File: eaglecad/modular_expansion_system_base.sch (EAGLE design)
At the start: 34 parts, among them IC1 74LS244N, IC10 74LS30N, IC2 74LS244N, IC3 74LS244N, IC4 SRAM, IC5 74LS30N, IC8 74LS00N, IC9 7805T, J1-INTERRUPTS INTERRUPTS, J1_ADDRESS_CON j1, J2-WAITS WAITS, J2_DATA_AND_POWER_CON j2, SW1 100SP3T1B1M6QE

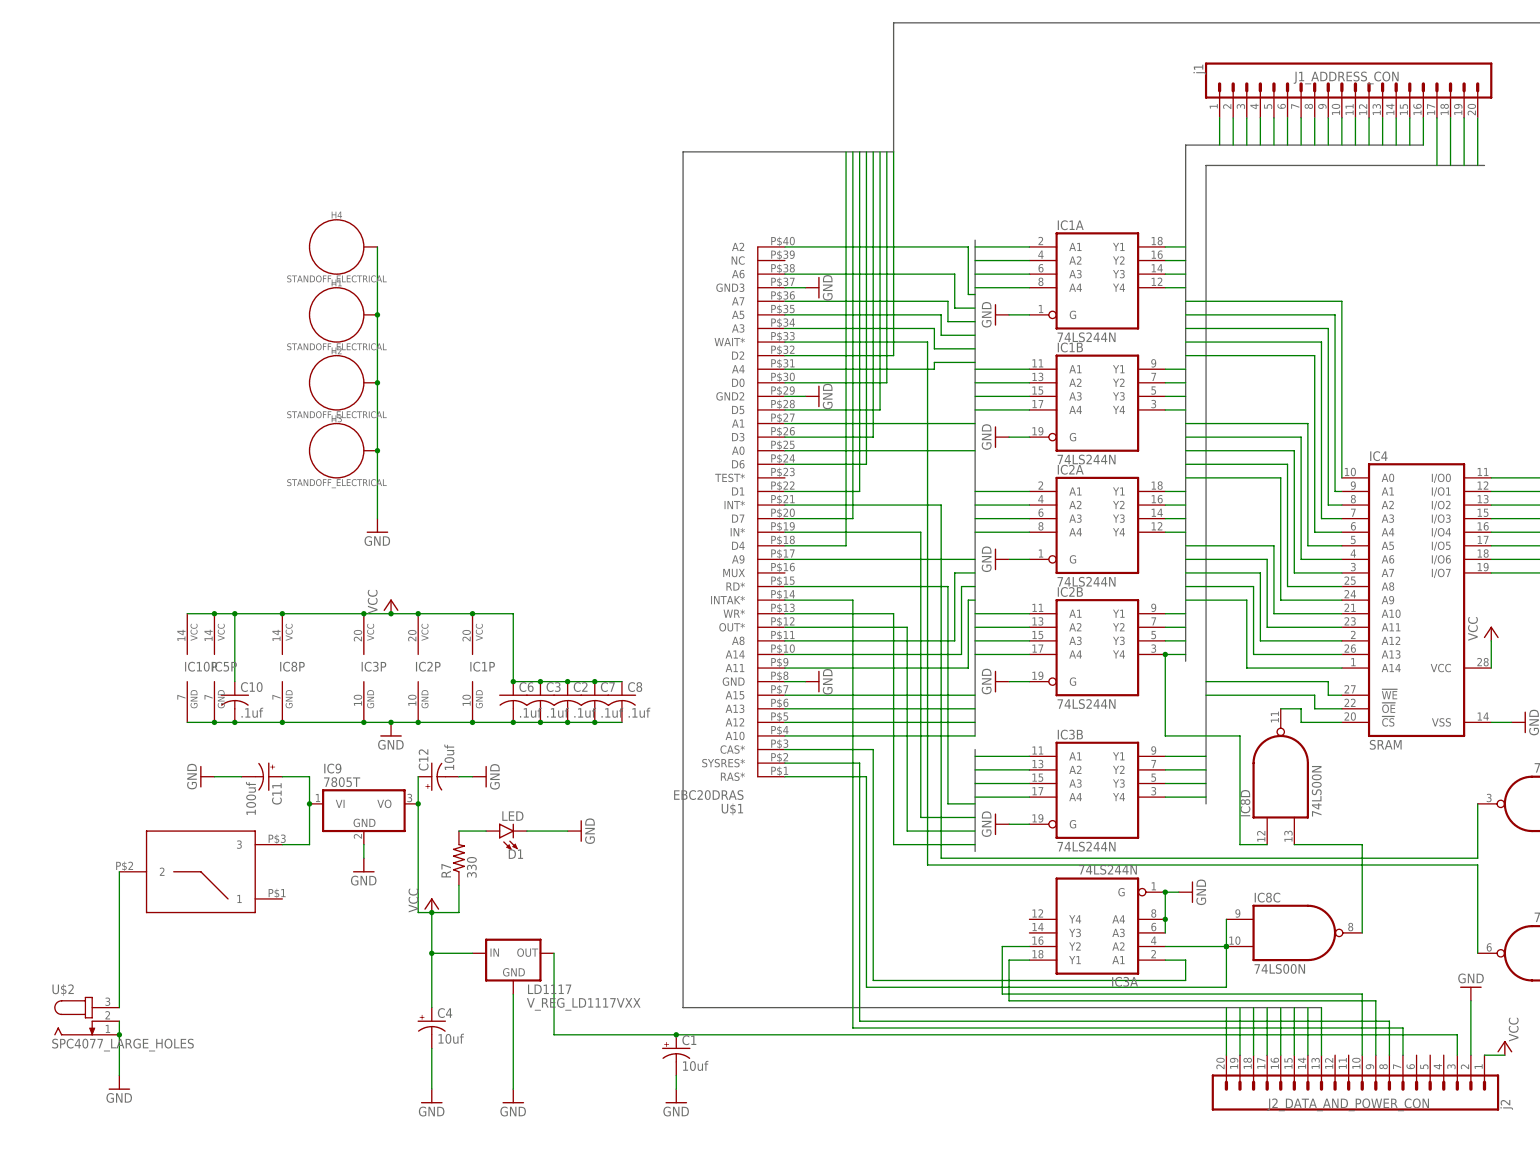
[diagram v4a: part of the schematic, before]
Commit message: added switching supply to base pcb
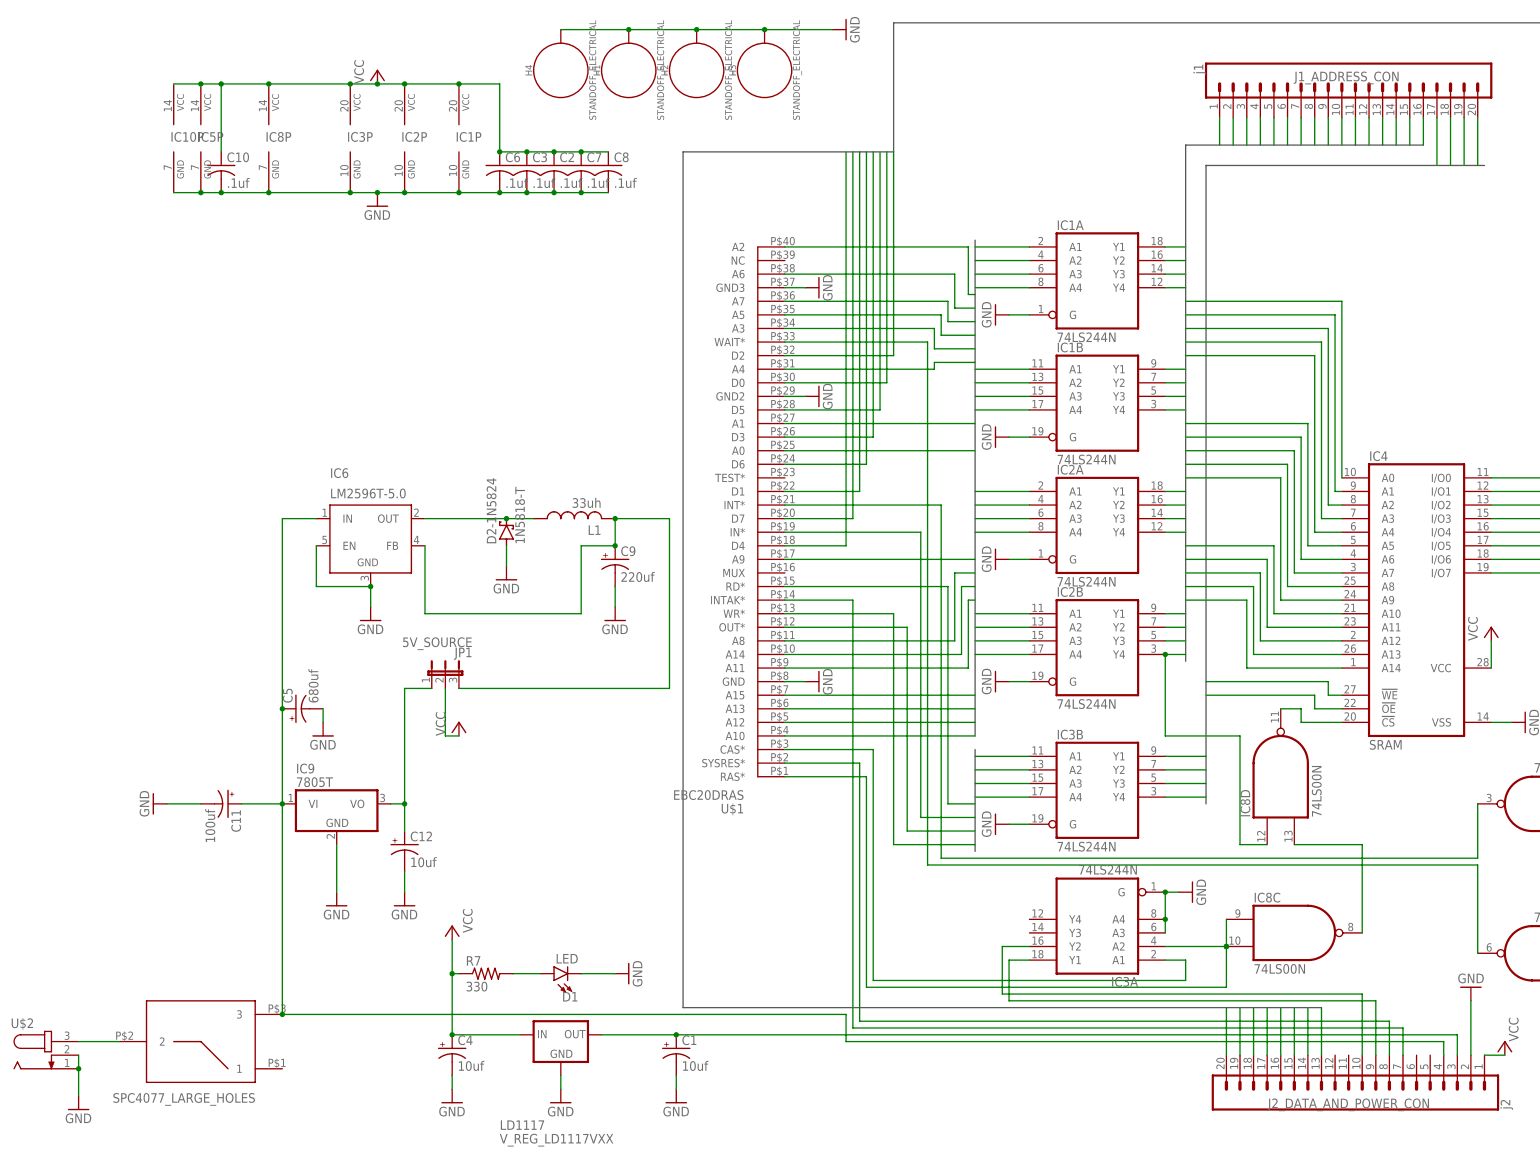
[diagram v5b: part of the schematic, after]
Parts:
- added C5: 680uf, rcl:CPOL-USE2.5-5
- added C9: 220uf, rcl:CPOL-USE2.5-5
- added D2-1N5824: 1N5818-T, diode:1N5818-T
- added IC6: LM2596T-5.0, linear:LM2596TH
- added JP1: 5V_SOURCE, jumper:JP2E
- added L1: 33uh, rcl:L-US6000-XXX-RC
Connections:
- net N$3 renamed 9V-IN
- removed net VOLTAGE-IN: C11.+, IC9.VI, SW1.3
- new net 5V_FROM_LINEAR_REG: C12.+, IC9.VO, JP1.1
- new net 5V_FROM_SWITCHER: C9.+, IC6.FB, JP1.3, L1.2
- new net 9V-POST-SW: C11.+, C5.+, IC6.IN, IC9.VI, J2_DATA_AND_POWER_CON.4, SW1.3
- new net N$1: D2-1N5824.C, IC6.OUT, L1.1
- net GND: now also C5.-, C9.-, D2-1N5824.A, IC6.EN, IC6.GND
- net VCC: now also JP1.2; no longer C12.+, IC9.VO
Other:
- moved on the sheet: C10, C11, C12, C2, C3, C4, C6, C7, C8, D1, H1, H2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

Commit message: updated schematics, boards, and pdfs
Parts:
- renumbered LD1117 to LD1117V33
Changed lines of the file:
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@@
 <setting verticaltext="up"/>
 </settings>
-<grid distance="0.05" unitdist="inch" unit="inch" style="lines" multiple="1" display="no" altdistance="0.005" altunitdist="inch" altunit="inch"/>
+<grid distance="0.1" unitdist="inch" unit="inch" style="lines" multiple="1" display="no" altdistance="0.01" altunitdist="inch" altunit="inch"/>
 <layers>
 <layer number="1" name="Top" color="4" fill="1" visible="no" active="no"/>
@@
 <part name="P+3" library="supply1" library_urn="urn:adsk.eagle:library:371" deviceset="VCC" device=""/>
 <part name="GND15" library="supply1" library_urn="urn:adsk.eagle:library:371" deviceset="GND" device=""/>
-<part name="LD1117" library="SparkFun-IC-Power" library_urn="urn:adsk.eagle:library:526" deviceset="V_REG_LD1117VXX" device="" package3d_urn="urn:adsk.eagle:package:39065/1"/>
+<part name="LD1117V33" library="SparkFun-IC-Power" library_urn="urn:adsk.eagle:library:526" deviceset="V_REG_LD1117VXX" device="" package3d_urn="urn:adsk.eagle:package:39065/1"/>
 <part name="GND16" library="supply1" library_urn="urn:adsk.eagle:library:371" deviceset="GND" device=""/>
 <part name="C1" library="resistor" library_urn="urn:adsk.eagle:library:348" deviceset="CPOL-US" device="E2.5-5" package3d_urn="urn:adsk.eagle:package:23344/1" value="10uf"/>
@@
 <attribute name="VALUE" x="270.51" y="29.21" size="1.778" layer="96" rot="R180"/>
 </instance>
-<instance part="LD1117" gate="G$1" x="97.79" y="17.78" smashed="yes">
+<instance part="LD1117V33" gate="G$1" x="97.79" y="17.78" smashed="yes">
 <attribute name="NAME" x="86.36" y="0" size="1.778" layer="95"/>
 <attribute name="VALUE" x="86.36" y="-2.54" size="1.778" layer="96"/>
@@
 </segment>
 <segment>
-<pinref part="LD1117" gate="G$1" pin="GND"/>
+<pinref part="LD1117V33" gate="G$1" pin="GND"/>
 <pinref part="GND16" gate="1" pin="GND"/>
 <wire x1="97.79" y1="10.16" x2="97.79" y2="7.62" width="0.1524" layer="91"/>
@@
 <pinref part="R7" gate="G$1" pin="1"/>
 <pinref part="C4" gate="G$1" pin="+"/>
-<pinref part="LD1117" gate="G$1" pin="IN"/>
+<pinref part="LD1117V33" gate="G$1" pin="IN"/>
 <wire x1="90.17" y1="17.78" x2="77.47" y2="17.78" width="0.1524" layer="91"/>
 <junction x="77.47" y="17.78"/>
@@
 <wire x1="265.43" y1="13.97" x2="265.43" y2="17.78" width="0.1524" layer="91"/>
 <wire x1="265.43" y1="17.78" x2="119.38" y2="17.78" width="0.1524" layer="91"/>
-<pinref part="LD1117" gate="G$1" pin="OUT"/>
+<pinref part="LD1117V33" gate="G$1" pin="OUT"/>
 <wire x1="119.38" y1="17.78" x2="105.41" y2="17.78" width="0.1524" layer="91"/>
 <pinref part="C1" gate="G$1" pin="+"/>

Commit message: added bill of materials
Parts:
- removed C5: 680uf, rcl:CPOL-USE2.5-5
- added C13: 680uf, rcl:CPOL-USE3.5-8
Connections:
- net 9V-POST-SW: now also C13.+; no longer C5.+
- net GND: now also C13.-; no longer C5.-
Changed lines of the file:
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@@
 <part name="IC6" library="linear" library_urn="urn:adsk.eagle:library:262" deviceset="LM2596T" device="H" package3d_urn="urn:adsk.eagle:package:16443/1" value="LM2596T-5.0"/>
 <part name="GND10" library="supply1" library_urn="urn:adsk.eagle:library:371" deviceset="GND" device=""/>
-<part name="C5" library="rcl" library_urn="urn:adsk.eagle:library:334" deviceset="CPOL-US" device="E2.5-5" package3d_urn="urn:adsk.eagle:package:23344/1" value="680uf"/>
 <part name="GND11" library="supply1" library_urn="urn:adsk.eagle:library:371" deviceset="GND" device=""/>
 <part name="D2-1N5824" library="diode" library_urn="urn:adsk.eagle:library:210" deviceset="1N581*" device="" package3d_urn="urn:adsk.eagle:package:43421/1" technology="8-T"/>
@@
 <part name="JP1" library="jumper" library_urn="urn:adsk.eagle:library:252" deviceset="JP2E" device="" package3d_urn="urn:adsk.eagle:package:15452/1" value="5V_SOURCE"/>
 <part name="P+7" library="supply1" library_urn="urn:adsk.eagle:library:371" deviceset="VCC" device=""/>
+<part name="C13" library="rcl" library_urn="urn:adsk.eagle:library:334" deviceset="CPOL-US" device="E3.5-8" package3d_urn="urn:adsk.eagle:package:23360/2" value="680uf"/>
 </parts>
 <sheets>
@@
 <attribute name="VALUE" x="59.69" y="92.71" size="1.778" layer="96"/>
 </instance>
-<instance part="C5" gate="G$1" x="48.26" y="78.74" smashed="yes" rot="R90">
-<attribute name="NAME" x="47.625" y="79.756" size="1.778" layer="95" rot="R90"/>
-<attribute name="VALUE" x="52.451" y="79.756" size="1.778" layer="96" rot="R90"/>
-</instance>
 <instance part="GND11" gate="1" x="53.34" y="73.66" smashed="yes">
 <attribute name="VALUE" x="50.8" y="71.12" size="1.778" layer="96"/>
@@
 <instance part="P+7" gate="VCC" x="78.74" y="76.2" smashed="yes">
 <attribute name="VALUE" x="76.2" y="73.66" size="1.778" layer="96" rot="R90"/>
+</instance>
+<instance part="C13" gate="G$1" x="48.26" y="88.9" smashed="yes" rot="R90">
+<attribute name="NAME" x="47.625" y="89.916" size="1.778" layer="95" rot="R90"/>
+<attribute name="VALUE" x="52.451" y="89.916" size="1.778" layer="96" rot="R90"/>
 </instance>
 </instances>
@@
 </segment>
 <segment>
-<pinref part="C5" gate="G$1" pin="-"/>
 <pinref part="GND11" gate="1" pin="GND"/>
 <wire x1="53.34" y1="78.74" x2="53.34" y2="76.2" width="0.1524" layer="91"/>
+<pinref part="C13" gate="G$1" pin="-"/>
+<wire x1="53.34" y1="88.9" x2="53.34" y2="76.2" width="0.1524" layer="91"/>
+<junction x="53.34" y="76.2"/>
 </segment>
 <segment>
@@
 <pinref part="IC6" gate="NC1" pin="IN"/>
 <wire x1="52.07" y1="114.3" x2="45.72" y2="114.3" width="0.1524" layer="91"/>
-<wire x1="45.72" y1="114.3" x2="45.72" y2="78.74" width="0.1524" layer="91"/>
-<pinref part="C5" gate="G$1" pin="+"/>
-<wire x1="45.72" y1="78.74" x2="45.72" y2="60.96" width="0.1524" layer="91"/>
-<junction x="45.72" y="78.74"/>
-</segment>
-</net>
+<wire x1="45.72" y1="114.3" x2="45.72" y2="88.9" width="0.1524" layer="91"/>
+<wire x1="45.72" y1="88.9" x2="45.72" y2="60.96" width="0.1524" layer="91"/>
+<pinref part="C13" gate="G$1" pin="+"/>
+<junction x="45.72" y="88.9"/>
+</segment>
+</net>

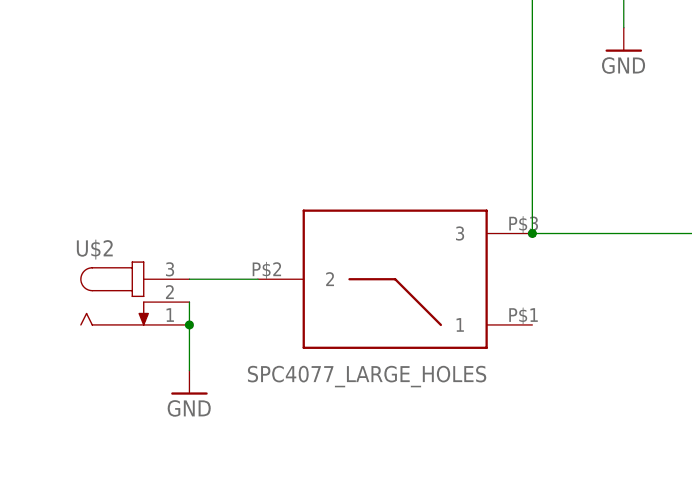
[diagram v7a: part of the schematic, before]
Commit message: implemented pacman fruit behavior
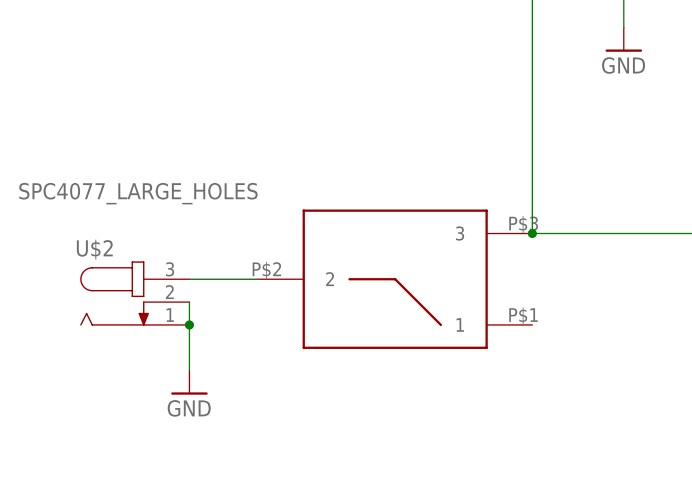
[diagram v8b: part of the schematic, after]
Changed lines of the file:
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@@
 <instance part="U$2" gate="G$1" x="2.54" y="13.97" smashed="yes">
 <attribute name="NAME" x="-5.08" y="19.05" size="1.778" layer="95"/>
-<attribute name="VALUE" x="13.97" y="5.08" size="1.778" layer="96"/>
+<attribute name="VALUE" x="-11.43" y="25.4" size="1.778" layer="96"/>
 </instance>
 <instance part="D1" gate="G$1" x="96.52" y="29.21" smashed="yes" rot="R90">
